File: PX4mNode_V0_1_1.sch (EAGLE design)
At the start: 133 parts, among them J201 DF13C-6P-1.25V, J202 DF13C-6P-1.25V, J203 DF13C-6P-1.25V, J301 DF13C-4P-1.25V, J401 DF13C-7P-1.25V, J402 DF13-4P-1.25V, J403 DF13C-4P-1.25V, J404 DF13C-4P-1.25V, J405 DF13C-4P-1.25V, J801 DF13C-3P-1.25V, M3_MOUNT1101 MOUNT-HOLE3.1MM, M3_MOUNT1102 MOUNT-HOLE3.1MM, M3_MOUNT1103 MOUNT-HOLE3.1MM, M3_MOUNT1104 MOUNT-HOLE3.1MM, U101 STM32F4X7VX, U401 MAX3051, U402 MAX3051, X101 3.2x2.5 mm / 24 MHz / 15 ppm

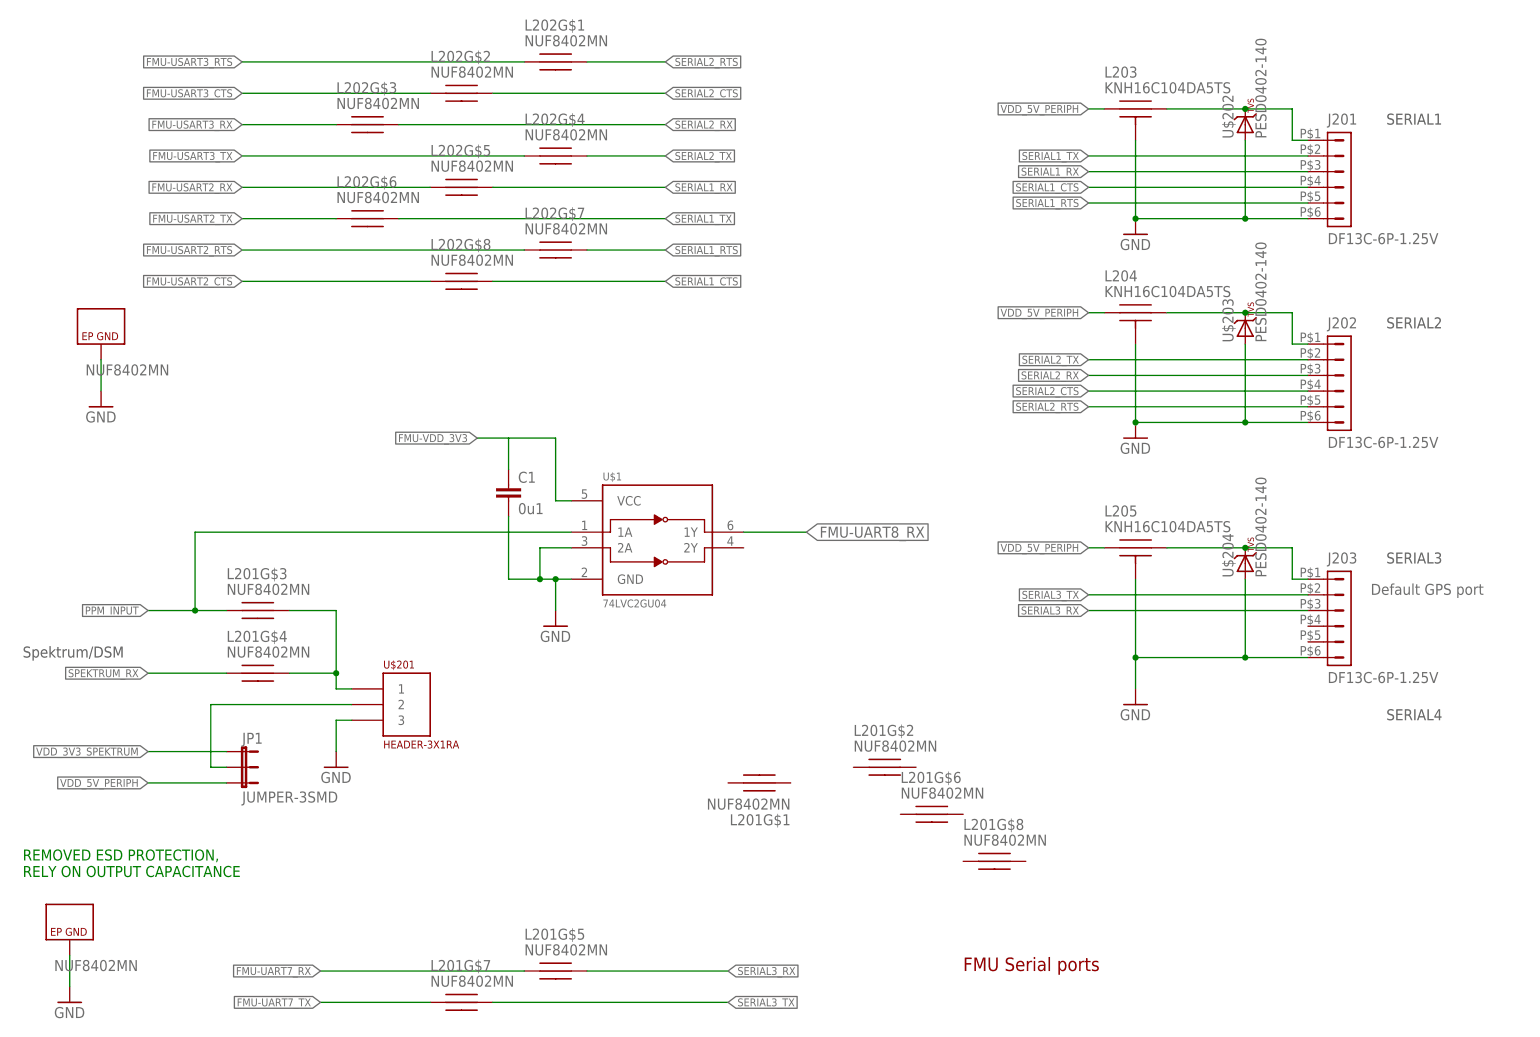
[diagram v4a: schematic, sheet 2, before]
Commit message: SBUS output fitted
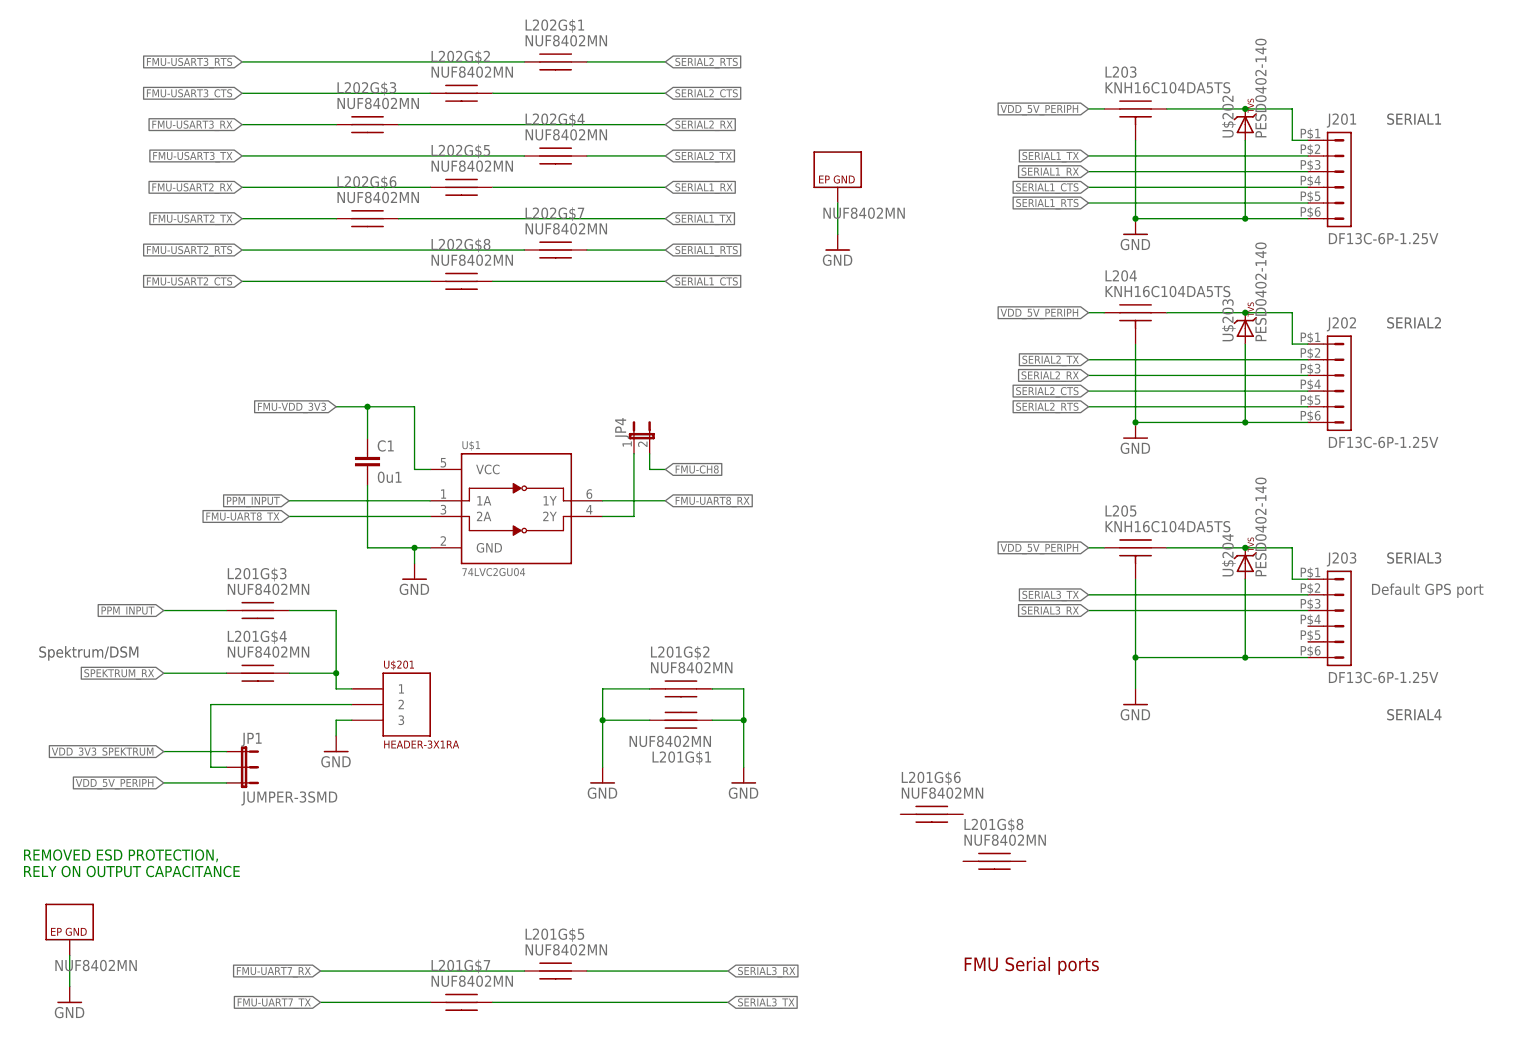
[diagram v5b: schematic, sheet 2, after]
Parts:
- added JP4: (no value), SparkFun-Passives:JUMPER-2SMD-NO
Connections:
- new net N$5: JP4.1, U$1.2Y
- net FMU-CH8: now also JP4.2
- net FMU-UART8_TX: now also U$1.2A
- net GND: now also L201G$1.P$1, L201G$1.P$2, L201G$2.P$1, L201G$2.P$2; no longer U$1.2A
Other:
- moved on the sheet: C1, L201G$1, L201G$2, U$1
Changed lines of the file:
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@@
 <attribute name="PARTNO" value="*"/>
 </part>
+<part name="JP4" library="SparkFun-Passives" deviceset="JUMPER-2" device="SMD-NO"/>
+<part name="GND19" library="pixhawk2" deviceset="GND" device=""/>
+<part name="GND22" library="pixhawk2" deviceset="GND" device=""/>
 </parts>
 <sheets>
@@
 <text x="233.68" y="58.42" size="1.778" layer="97">SERIAL4</text>
 <text x="231.14" y="78.74" size="1.778" layer="95">Default GPS port</text>
-<text x="12.7" y="68.58" size="1.778" layer="97">Spektrum/DSM</text>
+<text x="15.24" y="68.58" size="1.778" layer="97">Spektrum/DSM</text>
 <text x="12.7" y="33.02" size="1.778" layer="91">REMOVED ESD PROTECTION,
 RELY ON OUTPUT CAPACITANCE</text>
@@
 <instance part="L202" gate="G$7" x="99.06" y="134.62"/>
 <instance part="L202" gate="G$8" x="83.82" y="129.54"/>
-<instance part="L202" gate="G$9" x="25.4" y="116.84"/>
-<instance part="GND8" gate="1" x="25.4" y="109.22"/>
+<instance part="L202" gate="G$9" x="144.78" y="142.24"/>
+<instance part="GND8" gate="1" x="144.78" y="134.62"/>
 <instance part="L201" gate="G$9" x="20.32" y="20.32"/>
 <instance part="L201" gate="G$5" x="99.06" y="17.78"/>
@@
 <instance part="L201" gate="G$4" x="50.8" y="66.04"/>
 <instance part="GND9" gate="1" x="20.32" y="12.7"/>
-<instance part="GND46" gate="1" x="63.5" y="50.8"/>
+<instance part="GND46" gate="1" x="63.5" y="53.34"/>
 <instance part="U$201" gate="G$1" x="73.66" y="58.42"/>
-<instance part="L201" gate="G$1" x="132.08" y="48.26" rot="R180"/>
+<instance part="L201" gate="G$1" x="119.38" y="58.42" rot="R180"/>
 <instance part="L201" gate="G$6" x="160.02" y="43.18"/>
-<instance part="L201" gate="G$2" x="152.4" y="50.8"/>
+<instance part="L201" gate="G$2" x="119.38" y="63.5"/>
 <instance part="L201" gate="G$8" x="170.18" y="35.56"/>
-<instance part="U$1" gate="G$1" x="114.3" y="86.36"/>
-<instance part="GND2" gate="1" x="99.06" y="73.66"/>
-<instance part="C1" gate="G$1" x="91.44" y="93.98">
-<attribute name="PARTNO" x="91.44" y="93.98" size="1.778" layer="96" display="off"/>
+<instance part="U$1" gate="G$1" x="91.44" y="91.44"/>
+<instance part="GND2" gate="1" x="76.2" y="81.28"/>
+<instance part="C1" gate="G$1" x="68.58" y="99.06">
+<attribute name="PARTNO" x="68.58" y="99.06" size="1.778" layer="96" display="off"/>
 </instance>
 <instance part="JP1" gate="G$1" x="48.26" y="53.34" rot="R270"/>
+<instance part="JP4" gate="A" x="111.76" y="104.14"/>
+<instance part="GND19" gate="1" x="106.68" y="48.26"/>
+<instance part="GND22" gate="1" x="129.54" y="48.26"/>
 </instances>
 <busses>
@@
 <segment>
 <pinref part="GND8" gate="1" pin="GND"/>
-<wire x1="25.4" y1="111.76" x2="25.4" y2="116.84" width="0.1524" layer="91"/>
+<wire x1="144.78" y1="137.16" x2="144.78" y2="142.24" width="0.1524" layer="91"/>
 <pinref part="L202" gate="G$9" pin="GND"/>
 </segment>
@@
 <pinref part="U$201" gate="G$1" pin="3"/>
 <wire x1="66.04" y1="58.42" x2="63.5" y2="58.42" width="0.1524" layer="91"/>
-<wire x1="63.5" y1="58.42" x2="63.5" y2="53.34" width="0.1524" layer="91"/>
+<wire x1="63.5" y1="58.42" x2="63.5" y2="55.88" width="0.1524" layer="91"/>
 </segment>
 <segment>
 <pinref part="GND2" gate="1" pin="GND"/>
-<wire x1="99.06" y1="76.2" x2="99.06" y2="81.28" width="0.1524" layer="91"/>
+<wire x1="76.2" y1="83.82" x2="76.2" y2="86.36" width="0.1524" layer="91"/>
 <pinref part="U$1" gate="G$1" pin="GND"/>
-<wire x1="99.06" y1="81.28" x2="101.6" y2="81.28" width="0.1524" layer="91"/>
+<wire x1="76.2" y1="86.36" x2="78.74" y2="86.36" width="0.1524" layer="91"/>
 <pinref part="C1" gate="G$1" pin="2"/>
-<wire x1="91.44" y1="91.44" x2="91.44" y2="81.28" width="0.1524" layer="91"/>
-<wire x1="91.44" y1="81.28" x2="96.52" y2="81.28" width="0.1524" layer="91"/>
-<junction x="99.06" y="81.28"/>
-<pinref part="U$1" gate="G$1" pin="2A"/>
-<wire x1="96.52" y1="81.28" x2="99.06" y2="81.28" width="0.1524" layer="91"/>
-<wire x1="101.6" y1="86.36" x2="96.52" y2="86.36" width="0.1524" layer="91"/>
-<wire x1="96.52" y1="86.36" x2="96.52" y2="81.28" width="0.1524" layer="91"/>
-<junction x="96.52" y="81.28"/>
+<wire x1="68.58" y1="96.52" x2="68.58" y2="86.36" width="0.1524" layer="91"/>
+<wire x1="68.58" y1="86.36" x2="76.2" y2="86.36" width="0.1524" layer="91"/>
+<junction x="76.2" y="86.36"/>
+</segment>
+<segment>
+<wire x1="114.3" y1="63.5" x2="106.68" y2="63.5" width="0.1524" layer="91"/>
+<pinref part="GND19" gate="1" pin="GND"/>
+<wire x1="106.68" y1="63.5" x2="106.68" y2="58.42" width="0.1524" layer="91"/>
+<pinref part="L201" gate="G$1" pin="P$2"/>
+<wire x1="106.68" y1="58.42" x2="106.68" y2="50.8" width="0.1524" layer="91"/>
+<wire x1="114.3" y1="58.42" x2="106.68" y2="58.42" width="0.1524" layer="91"/>
+<junction x="106.68" y="58.42"/>
+<pinref part="L201" gate="G$2" pin="P$1"/>
+</segment>
+<segment>
+<pinref part="GND22" gate="1" pin="GND"/>
+<wire x1="129.54" y1="50.8" x2="129.54" y2="58.42" width="0.1524" layer="91"/>
+<pinref part="L201" gate="G$2" pin="P$2"/>
+<wire x1="129.54" y1="58.42" x2="129.54" y2="63.5" width="0.1524" layer="91"/>
+<wire x1="129.54" y1="63.5" x2="124.46" y2="63.5" width="0.1524" layer="91"/>
+<pinref part="L201" gate="G$1" pin="P$1"/>
+<wire x1="124.46" y1="58.42" x2="129.54" y2="58.42" width="0.1524" layer="91"/>
+<junction x="129.54" y="58.42"/>
 </segment>
 </net>
@@
 </segment>
 <segment>
-<wire x1="45.72" y1="48.26" x2="33.02" y2="48.26" width="0.1524" layer="91"/>
-<label x="33.02" y="48.26" size="1.27" layer="95" rot="R180" xref="yes"/>
+<wire x1="45.72" y1="48.26" x2="35.56" y2="48.26" width="0.1524" layer="91"/>
+<label x="35.56" y="48.26" size="1.27" layer="95" rot="R180" xref="yes"/>
 <pinref part="JP1" gate="G$1" pin="3"/>
 </segment>
@@
 <net name="SPEKTRUM_RX" class="0">
 <segment>
-<label x="33.02" y="66.04" size="1.27" layer="95" font="vector" rot="R180" xref="yes"/>
-<wire x1="45.72" y1="66.04" x2="33.02" y2="66.04" width="0.1524" layer="91"/>
+<label x="35.56" y="66.04" size="1.27" layer="95" font="vector" rot="R180" xref="yes"/>
+<wire x1="45.72" y1="66.04" x2="35.56" y2="66.04" width="0.1524" layer="91"/>
 <pinref part="L201" gate="G$4" pin="P$1"/>
 </segment>
@@
 <net name="VDD_3V3_SPEKTRUM" class="1">
 <segment>
-<label x="33.02" y="53.34" size="1.27" layer="95" rot="R180" xref="yes"/>
+<label x="35.56" y="53.34" size="1.27" layer="95" rot="R180" xref="yes"/>
 <pinref part="JP1" gate="G$1" pin="1"/>
-<wire x1="45.72" y1="53.34" x2="33.02" y2="53.34" width="0.1524" layer="91"/>
+<wire x1="45.72" y1="53.34" x2="35.56" y2="53.34" width="0.1524" layer="91"/>
 </segment>
 </net>
@@
 <net name="PPM_INPUT" class="0">
 <segment>
-<label x="33.02" y="76.2" size="1.27" layer="95" rot="R180" xref="yes"/>
-<wire x1="33.02" y1="76.2" x2="40.64" y2="76.2" width="0.1524" layer="91"/>
+<label x="35.56" y="76.2" size="1.27" layer="95" rot="R180" xref="yes"/>
+<wire x1="35.56" y1="76.2" x2="45.72" y2="76.2" width="0.1524" layer="91"/>
 <pinref part="L201" gate="G$3" pin="P$1"/>
+</segment>
+<segment>
+<label x="55.88" y="93.98" size="1.27" layer="95" rot="R180" xref="yes"/>
 <pinref part="U$1" gate="G$1" pin="1A"/>
-<wire x1="40.64" y1="76.2" x2="45.72" y2="76.2" width="0.1524" layer="91"/>
-<wire x1="101.6" y1="88.9" x2="40.64" y2="88.9" width="0.1524" layer="91"/>
-<wire x1="40.64" y1="88.9" x2="40.64" y2="76.2" width="0.1524" layer="91"/>
-<junction x="40.64" y="76.2"/>
+<wire x1="55.88" y1="93.98" x2="78.74" y2="93.98" width="0.1524" layer="91"/>
 </segment>
 </net>
@@
 <net name="FMU-VDD_3V3" class="1">
 <segment>
-<wire x1="101.6" y1="93.98" x2="99.06" y2="93.98" width="0.1524" layer="91"/>
-<wire x1="99.06" y1="93.98" x2="99.06" y2="104.14" width="0.1524" layer="91"/>
-<wire x1="99.06" y1="104.14" x2="91.44" y2="104.14" width="0.1524" layer="91"/>
-<label x="86.36" y="104.14" size="1.27" layer="95" rot="R180" xref="yes"/>
+<wire x1="78.74" y1="99.06" x2="76.2" y2="99.06" width="0.1524" layer="91"/>
+<wire x1="76.2" y1="99.06" x2="76.2" y2="109.22" width="0.1524" layer="91"/>
+<wire x1="76.2" y1="109.22" x2="68.58" y2="109.22" width="0.1524" layer="91"/>
+<label x="63.5" y="109.22" size="1.27" layer="95" rot="R180" xref="yes"/>
 <pinref part="U$1" gate="G$1" pin="VCC"/>
 <pinref part="C1" gate="G$1" pin="1"/>
-<wire x1="91.44" y1="104.14" x2="86.36" y2="104.14" width="0.1524" layer="91"/>
-<wire x1="91.44" y1="99.06" x2="91.44" y2="104.14" width="0.1524" layer="91"/>
+<wire x1="68.58" y1="109.22" x2="63.5" y2="109.22" width="0.1524" layer="91"/>
+<wire x1="68.58" y1="104.14" x2="68.58" y2="109.22" width="0.1524" layer="91"/>
+<junction x="68.58" y="109.22"/>
 </segment>
 </net>
@@
 <segment>
 <pinref part="U$1" gate="G$1" pin="1Y"/>
-<wire x1="129.54" y1="88.9" x2="139.7" y2="88.9" width="0.1524" layer="91"/>
-<label x="139.7" y="88.9" size="1.778" layer="95" xref="yes"/>
+<wire x1="106.68" y1="93.98" x2="116.84" y2="93.98" width="0.1524" layer="91"/>
+<label x="116.84" y="93.98" size="1.27" layer="95" xref="yes"/>
 </segment>
 </net>
@@
 </segment>
 </net>
+<net name="FMU-UART8_TX" class="0">
+<segment>
+<wire x1="78.74" y1="91.44" x2="55.88" y2="91.44" width="0.1524" layer="91"/>
+<label x="55.88" y="91.44" size="1.27" layer="95" rot="MR0" xref="yes"/>
+<pinref part="U$1" gate="G$1" pin="2A"/>
+</segment>
+</net>
+<net name="N$5" class="0">
+<segment>
+<pinref part="U$1" gate="G$1" pin="2Y"/>
+<wire x1="106.68" y1="91.44" x2="111.76" y2="91.44" width="0.1524" layer="91"/>
+<pinref part="JP4" gate="A" pin="1"/>
+<wire x1="111.76" y1="101.6" x2="111.76" y2="91.44" width="0.1524" layer="91"/>
+</segment>
+</net>
+<net name="FMU-CH8" class="0">
+<segment>
+<wire x1="114.3" y1="99.06" x2="116.84" y2="99.06" width="0.1524" layer="91"/>
+<pinref part="JP4" gate="A" pin="2"/>
+<wire x1="114.3" y1="99.06" x2="114.3" y2="101.6" width="0.1524" layer="91"/>
+<label x="116.84" y="99.06" size="1.27" layer="95" xref="yes"/>
+</segment>
+</net>

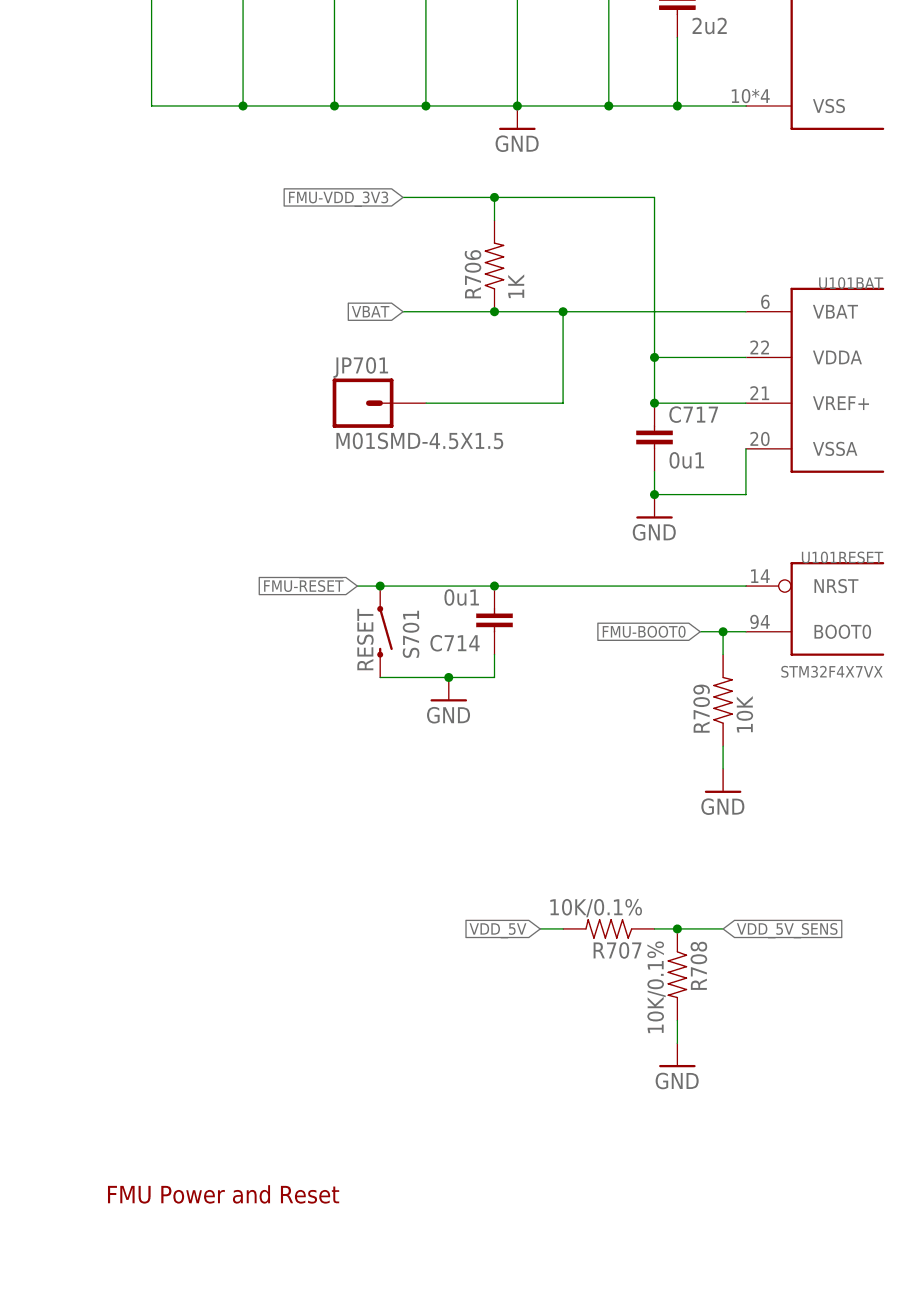
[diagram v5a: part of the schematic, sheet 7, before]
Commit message: Added schottky diode for VBAT charging
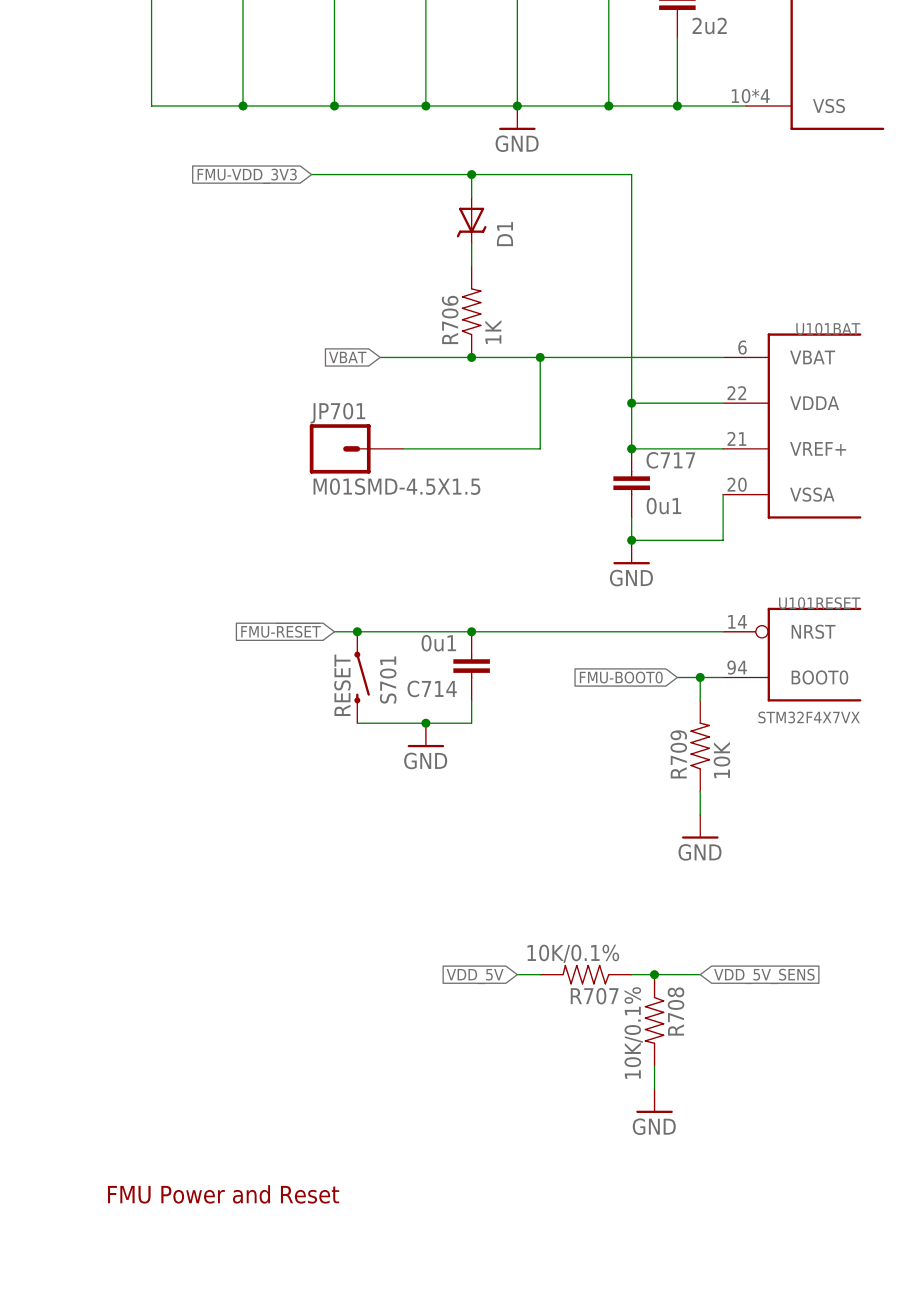
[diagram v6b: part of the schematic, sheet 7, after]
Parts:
- added D1: MSS1P4-M3, pixhawk2:DIODE-SCHOTTKY_MSMP
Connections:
- new net N$9: D1.C, R706.2
- net FMU-VDD_3V3: now also D1.A; no longer R706.2
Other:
- moved on the sheet: C714, C717, JP701, R706, R707, R708, R709, S701, U101BAT, U101RESET
